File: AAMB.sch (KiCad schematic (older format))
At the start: 13 parts, among them J1 Screw_Terminal_01x04, J2 PJRAS4X2U01X, J3 SPKR L, J4 SPKR R, J5 Screw_Terminal_01x03, J6 Screw_Terminal_01x03, J7 Screw_Terminal_01x04

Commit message: Some layout progress. Nightly commit.
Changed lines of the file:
@@
 EESchema Schematic File Version 4
-LIBS:AAMB-cache
 EELAYER 30 0
 EELAYER END
@@
 	2000 5100 2000 4600
 $Comp
-L power:25Vac #PWR0123
+L AAMB-rescue:25Vac-power #PWR0123
 U 1 1 5E3B1483
 P 1650 700
@@
 	900  1450 950  1450
 $Comp
-L power:25Vac #PWR0124
+L AAMB-rescue:25Vac-power #PWR0124
 U 1 1 5E3BCE97
 P 950 1375

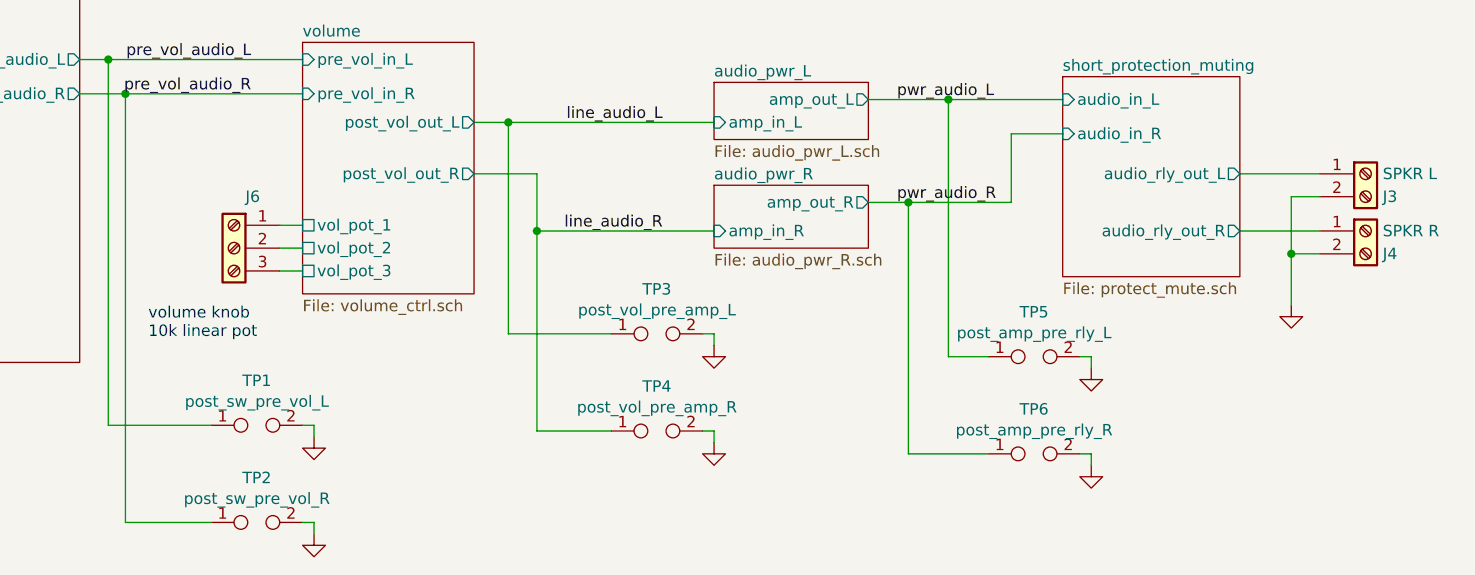
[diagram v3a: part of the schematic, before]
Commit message: Lots of part changes to SMD devices. Adding MPN, MFG to all parts for BOM export.
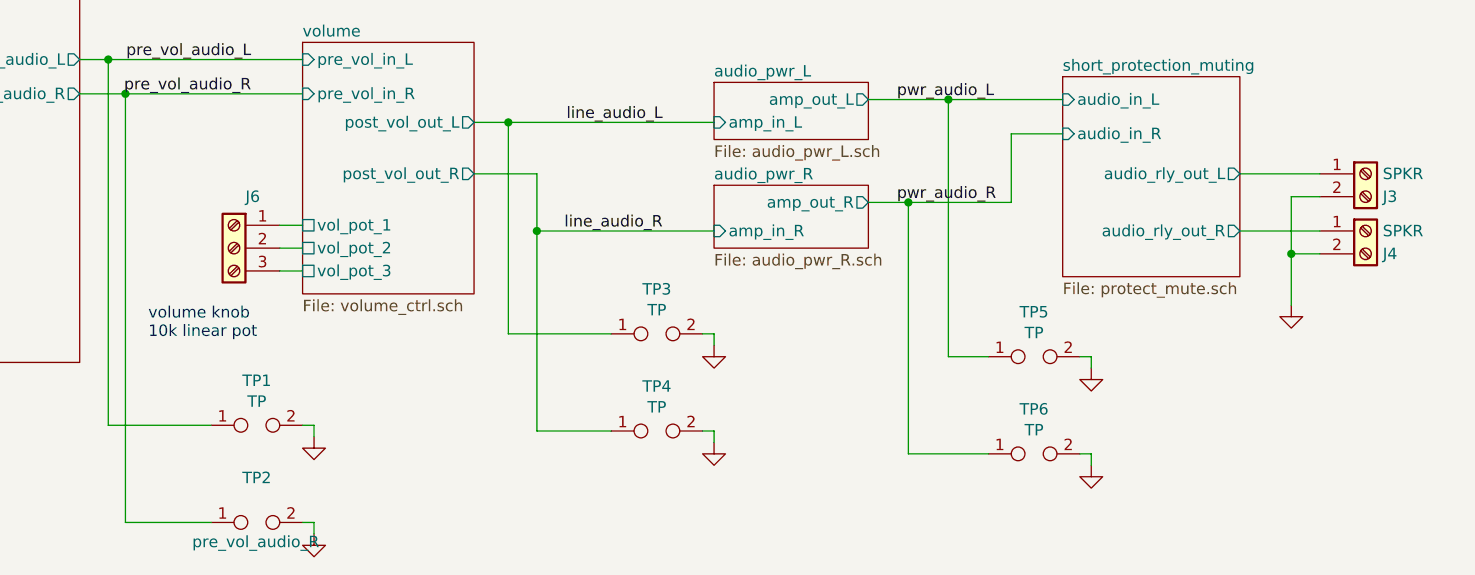
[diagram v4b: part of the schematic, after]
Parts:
- J1, J7: DigiKey (none) -> https://www.digikey.com/product-detail/en/cui-devices/TB001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; MFG (none) -> CUI Devices; MPN (none) -> TB001-500-04BE
- J2: DigiKey http://datasheets.diptrace.com/con_rca_jack/pjras4x2u__x_se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 -> https://www.digikey.com/product-detail/en/switchcraft-inc/P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; MFG (none) -> Switchcraft Inc.; MPN (none) -> PJRAS4X2U01X
- J3: value SPKR L -> SPKR; DigiKey https://www.digikey.com/product-detail/en/phoenix-contact/1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 -> https://media.digikey.com/pdf/Data%20Sheets/Phoenix%20Conta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; MFG (none) -> Phoenix Contact; MPN (none) -> 1935161
- J4: value SPKR R -> SPKR; DigiKey https://www.digikey.com/product-detail/en/phoenix-contact/1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 -> https://media.digikey.com/pdf/Data%20Sheets/Phoenix%20Conta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; MFG (none) -> Phoenix Contact; MPN (none) -> 1935161
- J5, J6: DigiKey (none) -> https://www.digikey.com/product-detail/en/phoenix-contact/1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; MFG (none) -> Phoenix Contact; MPN (none) -> 1935174
- TP1: value post_sw_pre_vol_L -> TP
- TP2: value post_sw_pre_vol_R -> TP; Note (none) -> pre_vol_audio_R
- TP3: value post_vol_pre_amp_L -> TP
- TP4: value post_vol_pre_amp_R -> TP
- TP5: value post_amp_pre_rly_L -> TP
- TP6: value post_amp_pre_rly_R -> TP
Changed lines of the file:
@@
 F 1 "PJRAS4X2U01X" H 1525 3775 50  0001 L BNN
 F 2 "Connectors-amp:PJRAS4X2U01X" H 1525 3850 50  0001 L BNN
-F 3 "" H 1725 3600 50  0001 L BNN
+F 3 "http://www.switchcraft.com/Drawings/pjras4x2u__x_series_cd.pdf" H 1725 3600 50  0001 L BNN
 F 4 "" H 1525 3300 50  0001 L BNN "Field4"
-F 5 "http://datasheets.diptrace.com/con_rca_jack/pjras4x2u__x_series_cd.pdf" H 1800 3500 50  0001 C CNN "DigiKey"
+F 5 "https://www.digikey.com/product-detail/en/switchcraft-inc/PJRAS4X2U01X/SC1537-ND/1289095?utm_adgroup=Barrel%20-%20Audio%20Connectors&utm_source=google&utm_medium=cpc&utm_campaign=Shopping_Connectors%2C%20Interconnects_NEW&utm_term=&utm_content=Barrel%20-%20Audio%20Connectors&gclid=CjwKCAjw7LX0BRBiEiwA__gNw-m2KtOPxMMQirDxre9hdMI7n4u67jcnrS7_d8-2Y6lwXiGIujj8URoCMcYQAvD_BwE" H 1800 3500 50  0001 C CNN "DigiKey"
+F 6 "Switchcraft Inc." H 1800 3500 50  0001 C CNN "MFG"
+F 7 "PJRAS4X2U01X" H 1800 3500 50  0001 C CNN "MPN"
 	1    1800 3500
 	1    0    0    -1
@@
 F 1 "PJRAS4X2U01X" H 1525 4275 50  0001 L BNN
 F 2 "Connectors-amp:PJRAS4X2U01X" H 1525 4350 50  0001 L BNN
-F 3 "" H 1725 4100 50  0001 L BNN
+F 3 "http://www.switchcraft.com/Drawings/pjras4x2u__x_series_cd.pdf" H 1725 4100 50  0001 L BNN
 F 4 "" H 1525 3800 50  0001 L BNN "Field4"
-F 5 "http://datasheets.diptrace.com/con_rca_jack/pjras4x2u__x_series_cd.pdf" H 1800 4000 50  0001 C CNN "DigiKey"
+F 5 "https://www.digikey.com/product-detail/en/switchcraft-inc/PJRAS4X2U01X/SC1537-ND/1289095?utm_adgroup=Barrel%20-%20Audio%20Connectors&utm_source=google&utm_medium=cpc&utm_campaign=Shopping_Connectors%2C%20Interconnects_NEW&utm_term=&utm_content=Barrel%20-%20Audio%20Connectors&gclid=CjwKCAjw7LX0BRBiEiwA__gNw-m2KtOPxMMQirDxre9hdMI7n4u67jcnrS7_d8-2Y6lwXiGIujj8URoCMcYQAvD_BwE" H 1800 4000 50  0001 C CNN "DigiKey"
+F 6 "Switchcraft Inc." H 1800 4000 50  0001 C CNN "MFG"
+F 7 "PJRAS4X2U01X" H 1800 4000 50  0001 C CNN "MPN"
 	2    1800 4000
 	1    0    0    -1
@@
 F 1 "PJRAS4X2U01X" H 1525 4775 50  0001 L BNN
 F 2 "Connectors-amp:PJRAS4X2U01X" H 1525 4850 50  0001 L BNN
-F 3 "" H 1725 4600 50  0001 L BNN
+F 3 "http://www.switchcraft.com/Drawings/pjras4x2u__x_series_cd.pdf" H 1725 4600 50  0001 L BNN
 F 4 "" H 1525 4300 50  0001 L BNN "Field4"
-F 5 "http://datasheets.diptrace.com/con_rca_jack/pjras4x2u__x_series_cd.pdf" H 1800 4500 50  0001 C CNN "DigiKey"
+F 5 "https://www.digikey.com/product-detail/en/switchcraft-inc/PJRAS4X2U01X/SC1537-ND/1289095?utm_adgroup=Barrel%20-%20Audio%20Connectors&utm_source=google&utm_medium=cpc&utm_campaign=Shopping_Connectors%2C%20Interconnects_NEW&utm_term=&utm_content=Barrel%20-%20Audio%20Connectors&gclid=CjwKCAjw7LX0BRBiEiwA__gNw-m2KtOPxMMQirDxre9hdMI7n4u67jcnrS7_d8-2Y6lwXiGIujj8URoCMcYQAvD_BwE" H 1800 4500 50  0001 C CNN "DigiKey"
+F 6 "Switchcraft Inc." H 1800 4500 50  0001 C CNN "MFG"
+F 7 "PJRAS4X2U01X" H 1800 4500 50  0001 C CNN "MPN"
 	3    1800 4500
 	1    0    0    -1
@@
 F 1 "PJRAS4X2U01X" H 1525 5275 50  0001 L BNN
 F 2 "Connectors-amp:PJRAS4X2U01X" H 1525 5350 50  0001 L BNN
-F 3 "" H 1725 5100 50  0001 L BNN
+F 3 "http://www.switchcraft.com/Drawings/pjras4x2u__x_series_cd.pdf" H 1725 5100 50  0001 L BNN
 F 4 "" H 1525 4800 50  0001 L BNN "Field4"
-F 5 "http://datasheets.diptrace.com/con_rca_jack/pjras4x2u__x_series_cd.pdf" H 1800 5000 50  0001 C CNN "DigiKey"
+F 5 "https://www.digikey.com/product-detail/en/switchcraft-inc/PJRAS4X2U01X/SC1537-ND/1289095?utm_adgroup=Barrel%20-%20Audio%20Connectors&utm_source=google&utm_medium=cpc&utm_campaign=Shopping_Connectors%2C%20Interconnects_NEW&utm_term=&utm_content=Barrel%20-%20Audio%20Connectors&gclid=CjwKCAjw7LX0BRBiEiwA__gNw-m2KtOPxMMQirDxre9hdMI7n4u67jcnrS7_d8-2Y6lwXiGIujj8URoCMcYQAvD_BwE" H 1800 5000 50  0001 C CNN "DigiKey"
+F 6 "Switchcraft Inc." H 1800 5000 50  0001 C CNN "MFG"
+F 7 "PJRAS4X2U01X" H 1800 5000 50  0001 C CNN "MPN"
 	4    1800 5000
 	1    0    0    -1
@@
 P 9800 4175
 F 0 "J4" H 9875 4075 50  0000 L CNN
-F 1 "SPKR R" H 9875 4175 50  0000 L CNN
+F 1 "SPKR" H 9875 4175 50  0000 L CNN
 F 2 "TerminalBlock_Phoenix:TerminalBlock_Phoenix_MKDS-1,5-2_1x02_P5.00mm_Horizontal" H 9800 4175 50  0001 C CNN
-F 3 "" H 9800 4175 50  0001 C CNN
-F 4 "https://www.digikey.com/product-detail/en/phoenix-contact/1715022/277-1258-ND/260626" H 9800 4175 50  0001 C CNN "DigiKey"
+F 3 "https://media.digikey.com/pdf/Data%20Sheets/Phoenix%20Contact%20PDFs/1935161.pdf" H 9800 4175 50  0001 C CNN
+F 4 "https://media.digikey.com/pdf/Data%20Sheets/Phoenix%20Contact%20PDFs/1935161.pdf" H 9800 4175 50  0001 C CNN "DigiKey"
+F 5 "Phoenix Contact" H 9800 4175 50  0001 C CNN "MFG"
+F 6 "1935161" H 9800 4175 50  0001 C CNN "MPN"
 	1    9800 4175
 	1    0    0    -1
@@
 F 1 "Screw_Terminal_01x04" H 618 1776 50  0001 C CNN
 F 2 "TerminalBlock_Phoenix:TerminalBlock_Phoenix_MKDS-1,5-4_1x04_P5.00mm_Horizontal" H 700 1550 50  0001 C CNN
-F 3 "https://www.digikey.com/product-detail/en/phoenix-contact/1729034/277-1238-ND/260606" H 700 1550 50  0001 C CNN
+F 3 "https://www.cuidevices.com/product/resource/tb001-500.pdf" H 700 1550 50  0001 C CNN
+F 4 "https://www.digikey.com/product-detail/en/cui-devices/TB001-500-04BE/102-6136-ND/10064060" H 700 1550 50  0001 C CNN "DigiKey"
+F 5 "CUI Devices" H 700 1550 50  0001 C CNN "MFG"
+F 6 "TB001-500-04BE" H 700 1550 50  0001 C CNN "MPN"
 	1    700  1550
 	-1   0    0    -1
@@
 F 1 "Screw_Terminal_01x03" H 1493 1826 50  0001 C CNN
 F 2 "TerminalBlock_Phoenix:TerminalBlock_Phoenix_MKDS-1,5-3_1x03_P5.00mm_Horizontal" H 1575 1600 50  0001 C CNN
-F 3 "~" H 1575 1600 50  0001 C CNN
+F 3 "https://media.digikey.com/pdf/Data%20Sheets/Phoenix%20Contact%20PDFs/1935174.pdf" H 1575 1600 50  0001 C CNN
+F 4 "https://www.digikey.com/product-detail/en/phoenix-contact/1935174/277-1578-ND/568615" H 1575 1600 50  0001 C CNN "DigiKey"
+F 5 "Phoenix Contact" H 1575 1600 50  0001 C CNN "MFG"
+F 6 "1935174" H 1575 1600 50  0001 C CNN "MPN"
 	1    1575 1600
 	-1   0    0    -1
@@
 F 1 "Screw_Terminal_01x03" H 4768 4476 50  0001 C CNN
 F 2 "TerminalBlock_Phoenix:TerminalBlock_Phoenix_MKDS-1,5-3_1x03_P5.00mm_Horizontal" H 4850 4250 50  0001 C CNN
-F 3 "~" H 4850 4250 50  0001 C CNN
+F 3 "https://media.digikey.com/pdf/Data%20Sheets/Phoenix%20Contact%20PDFs/1935174.pdf" H 4850 4250 50  0001 C CNN
+F 4 "https://www.digikey.com/product-detail/en/phoenix-contact/1935174/277-1578-ND/568615" H 4850 4250 50  0001 C CNN "DigiKey"
+F 5 "Phoenix Contact" H 4850 4250 50  0001 C CNN "MFG"
+F 6 "1935174" H 4850 4250 50  0001 C CNN "MPN"
 	1    4850 4250
 	-1   0    0    -1
@@
 P 4950 5025
 F 0 "TP1" H 4950 5220 50  0000 C CNN
-F 1 "post_sw_pre_vol_L" H 4950 5129 50  0000 C CNN
+F 1 "TP" H 4950 5129 50  0000 C CNN
 F 2 "TestPoint:TestPoint_2Pads_Pitch2.54mm_Drill0.8mm" H 4950 5025 50  0001 C CNN
 F 3 "~" H 4950 5025 50  0001 C CNN
@@
 P 4950 5450
 F 0 "TP2" H 4950 5645 50  0000 C CNN
-F 1 "post_sw_pre_vol_R" H 4950 5554 50  0000 C CNN
+F 1 "TP" H 4950 5554 50  0001 C CNN
 F 2 "TestPoint:TestPoint_2Pads_Pitch2.54mm_Drill0.8mm" H 4950 5450 50  0001 C CNN
 F 3 "~" H 4950 5450 50  0001 C CNN
+F 4 "pre_vol_audio_R" H 4945 5365 50  0000 C CNN "Note"
 	1    4950 5450
 	1    0    0    -1
@@
 P 6700 4625
 F 0 "TP3" H 6700 4820 50  0000 C CNN
-F 1 "post_vol_pre_amp_L" H 6700 4729 50  0000 C CNN
+F 1 "TP" H 6700 4729 50  0000 C CNN
 F 2 "TestPoint:TestPoint_2Pads_Pitch2.54mm_Drill0.8mm" H 6700 4625 50  0001 C CNN
 F 3 "~" H 6700 4625 50  0001 C CNN
@@
 P 6700 5050
 F 0 "TP4" H 6700 5245 50  0000 C CNN
-F 1 "post_vol_pre_amp_R" H 6700 5154 50  0000 C CNN
+F 1 "TP" H 6700 5154 50  0000 C CNN
 F 2 "TestPoint:TestPoint_2Pads_Pitch2.54mm_Drill0.8mm" H 6700 5050 50  0001 C CNN
 F 3 "~" H 6700 5050 50  0001 C CNN
@@
 P 8350 4725
 F 0 "TP5" H 8350 4920 50  0000 C CNN
-F 1 "post_amp_pre_rly_L" H 8350 4829 50  0000 C CNN
+F 1 "TP" H 8350 4829 50  0000 C CNN
 F 2 "TestPoint:TestPoint_2Pads_Pitch2.54mm_Drill0.8mm" H 8350 4725 50  0001 C CNN
 F 3 "~" H 8350 4725 50  0001 C CNN
@@
 P 8350 5150
 F 0 "TP6" H 8350 5345 50  0000 C CNN
-F 1 "post_amp_pre_rly_R" H 8350 5254 50  0000 C CNN
+F 1 "TP" H 8350 5254 50  0000 C CNN
 F 2 "TestPoint:TestPoint_2Pads_Pitch2.54mm_Drill0.8mm" H 8350 5150 50  0001 C CNN
 F 3 "~" H 8350 5150 50  0001 C CNN
@@
 F 1 "Screw_Terminal_01x04" H 2618 4676 50  0001 C CNN
 F 2 "TerminalBlock_Phoenix:TerminalBlock_Phoenix_MKDS-1,5-4_1x04_P5.00mm_Horizontal" H 2700 4450 50  0001 C CNN
-F 3 "~" H 2700 4450 50  0001 C CNN
+F 3 "https://www.cuidevices.com/product/resource/tb001-500.pdf" H 2700 4450 50  0001 C CNN
+F 4 "https://www.digikey.com/product-detail/en/cui-devices/TB001-500-04BE/102-6136-ND/10064060" H 2700 4450 50  0001 C CNN "DigiKey"
+F 5 "CUI Devices" H 2700 4450 50  0001 C CNN "MFG"
+F 6 "TB001-500-04BE" H 2700 4450 50  0001 C CNN "MPN"
 	1    2700 4450
 	-1   0    0    -1
@@
 P 9800 3925
 F 0 "J3" H 9875 3825 50  0000 L CNN
-F 1 "SPKR L" H 9875 3925 50  0000 L CNN
+F 1 "SPKR" H 9875 3925 50  0000 L CNN
 F 2 "TerminalBlock_Phoenix:TerminalBlock_Phoenix_MKDS-1,5-2_1x02_P5.00mm_Horizontal" H 9800 3925 50  0001 C CNN
-F 3 "" H 9800 3925 50  0001 C CNN
-F 4 "https://www.digikey.com/product-detail/en/phoenix-contact/1715022/277-1258-ND/260626" H 9800 3925 50  0001 C CNN "DigiKey"
+F 3 "https://media.digikey.com/pdf/Data%20Sheets/Phoenix%20Contact%20PDFs/1935161.pdf" H 9800 3925 50  0001 C CNN
+F 4 "https://media.digikey.com/pdf/Data%20Sheets/Phoenix%20Contact%20PDFs/1935161.pdf" H 9800 3925 50  0001 C CNN "DigiKey"
+F 5 "Phoenix Contact" H 9800 3925 50  0001 C CNN "MFG"
+F 6 "1935161" H 9800 3925 50  0001 C CNN "MPN"
 	1    9800 3925
 	1    0    0    -1
